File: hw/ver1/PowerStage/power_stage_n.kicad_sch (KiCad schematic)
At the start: 15 parts, among them Q1 MCAC80N10Y, Q2 MCAC80N10Y, U6 HIP2210

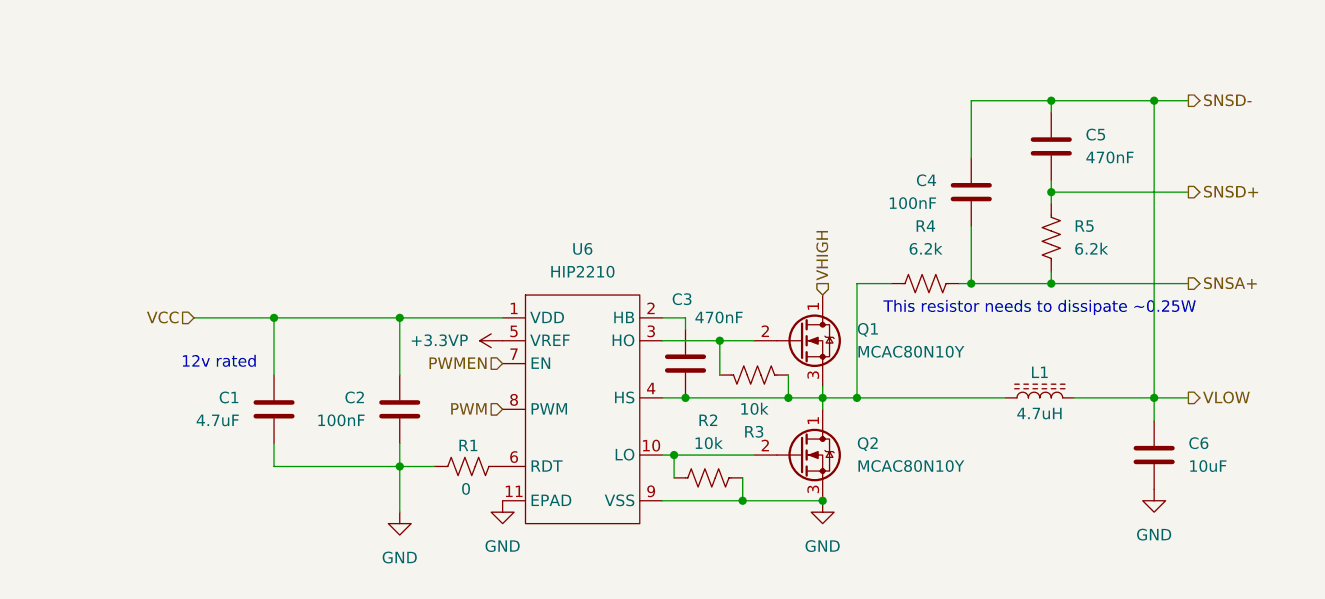
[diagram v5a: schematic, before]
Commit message: Mess with the buck design. Tear out previous approach.
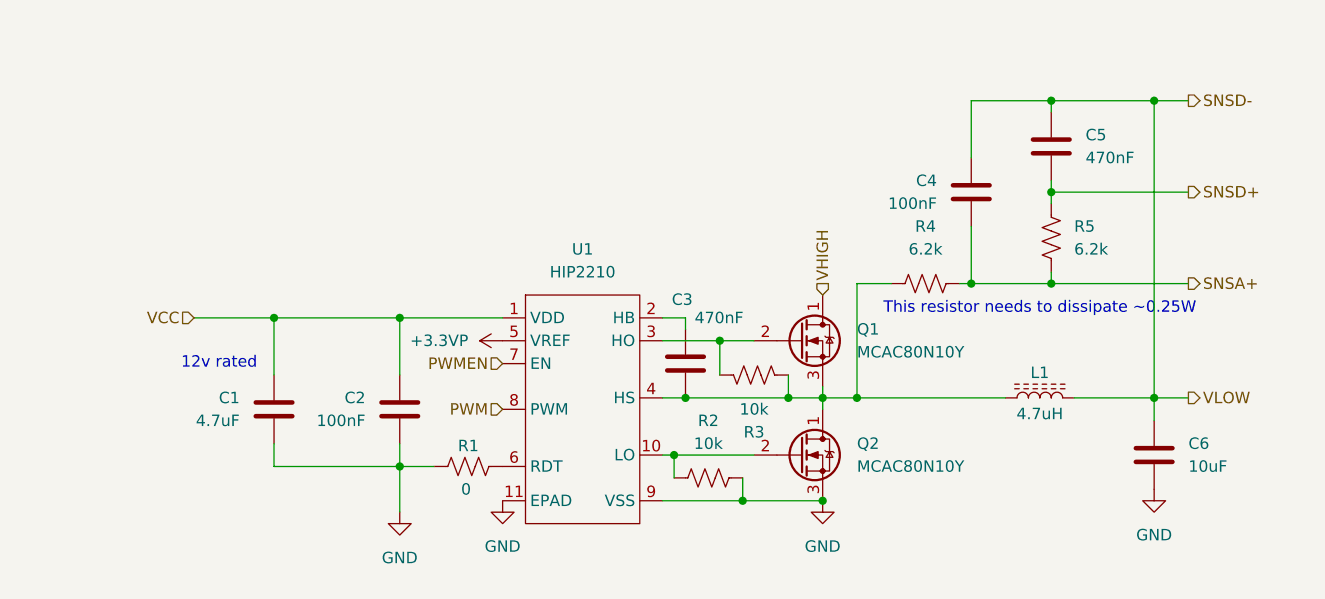
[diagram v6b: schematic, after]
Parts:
- U1: renamed from U6; footprint Package_DFN_QFN:TDFN-10-1EP_2x3mm_P0.5mm_EP0.9x2mm_ThermalVias -> DFN:TDFN-10-1EP_4x4mm_P0.8mm_EP2.6x3mm
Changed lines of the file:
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@@
 		(on_board yes)
 		(dnp no)
-		(fields_autoplaced yes)
 		(property "Reference" "Q1"
 			(at 172.72 69.8499 0)
@@
 		(dnp no)
 		(fields_autoplaced yes)
-		(property "Reference" "U6"
+		(property "Reference" "U1"
 			(at 142.24 60.96 0)
 			(effects
@@
 			)
 		)
-		(property "Footprint" "Package_DFN_QFN:TDFN-10-1EP_2x3mm_P0.5mm_EP0.9x2mm_ThermalVias"
+		(property "Footprint" "DFN:TDFN-10-1EP_4x4mm_P0.8mm_EP2.6x3mm"
 			(at 141.986 99.314 0)
 			(effects

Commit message: Sync work to laptop
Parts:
- added R80, R86: 10k, Resistor_SMD:R_0603_1608Metric, symbol Device:R_US
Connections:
- net GND: now also R86.2
- net VCC: now also R80.2
- net +3.3VP: no longer names the net of U1.5 (VREF)
- net +3.3VP: now also R80.1, R86.1
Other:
- note added: "VREF assumes 10V +VSW input for 5V PWM logic."
- note removed: "12v rated"
- moved on the sheet: C1, C2
